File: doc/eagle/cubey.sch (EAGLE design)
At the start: 25 parts, among them K1 PIN20X2

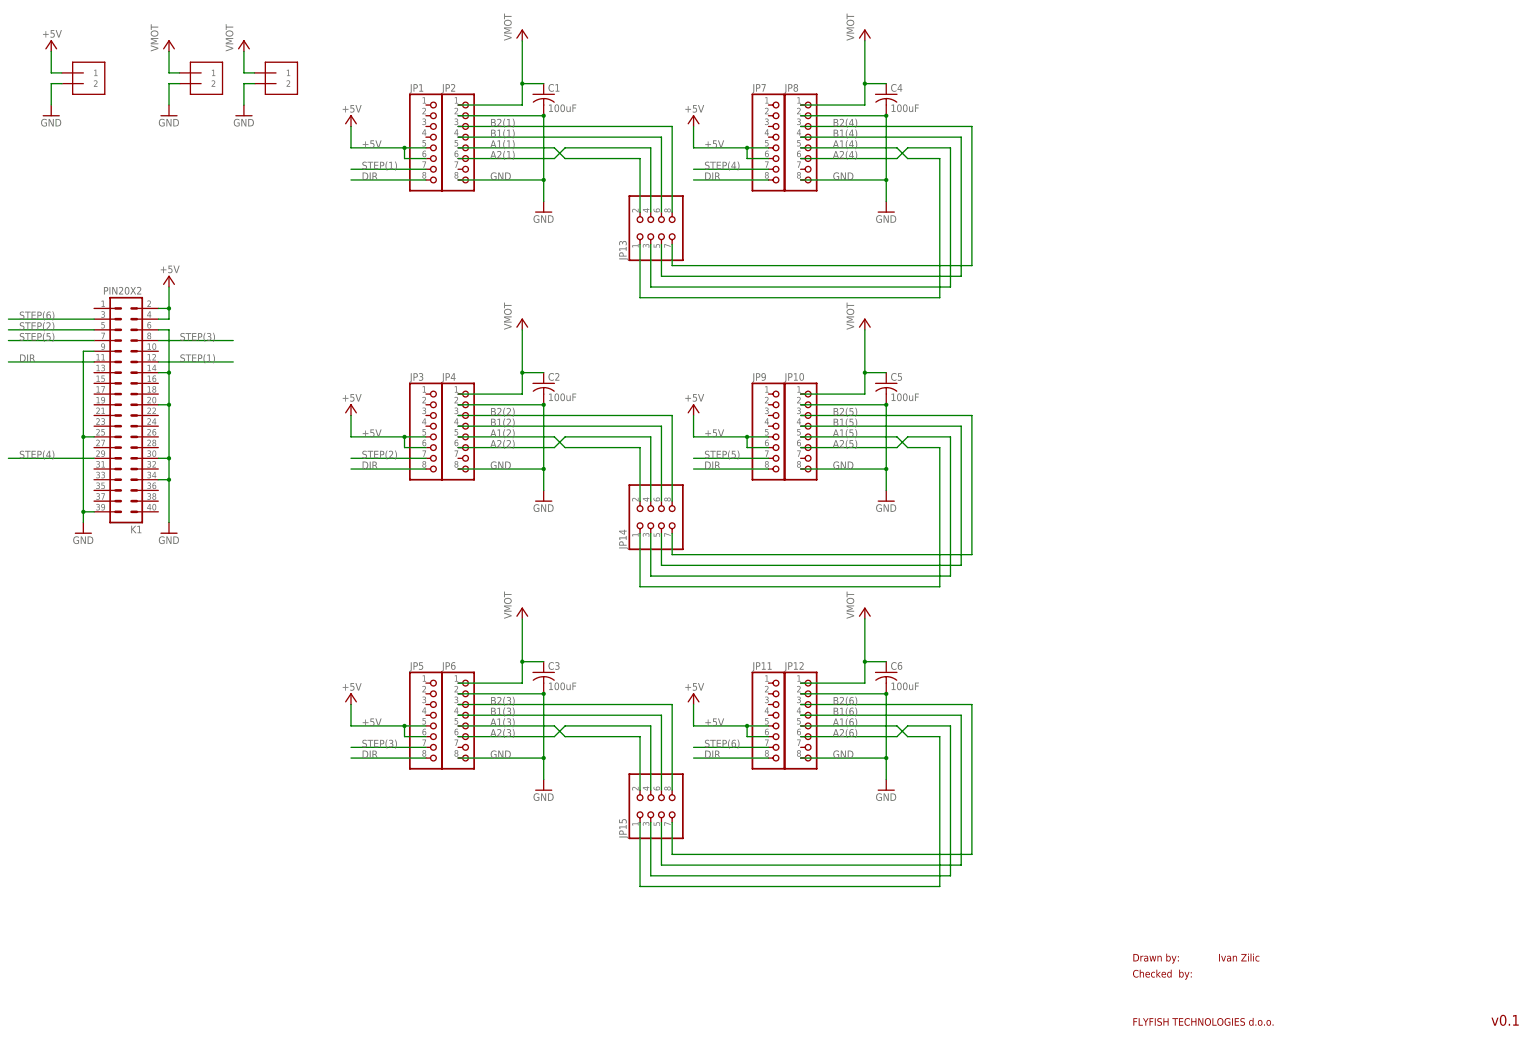
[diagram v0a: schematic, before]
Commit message: Added Solder jumpers for M0, M1 and M2
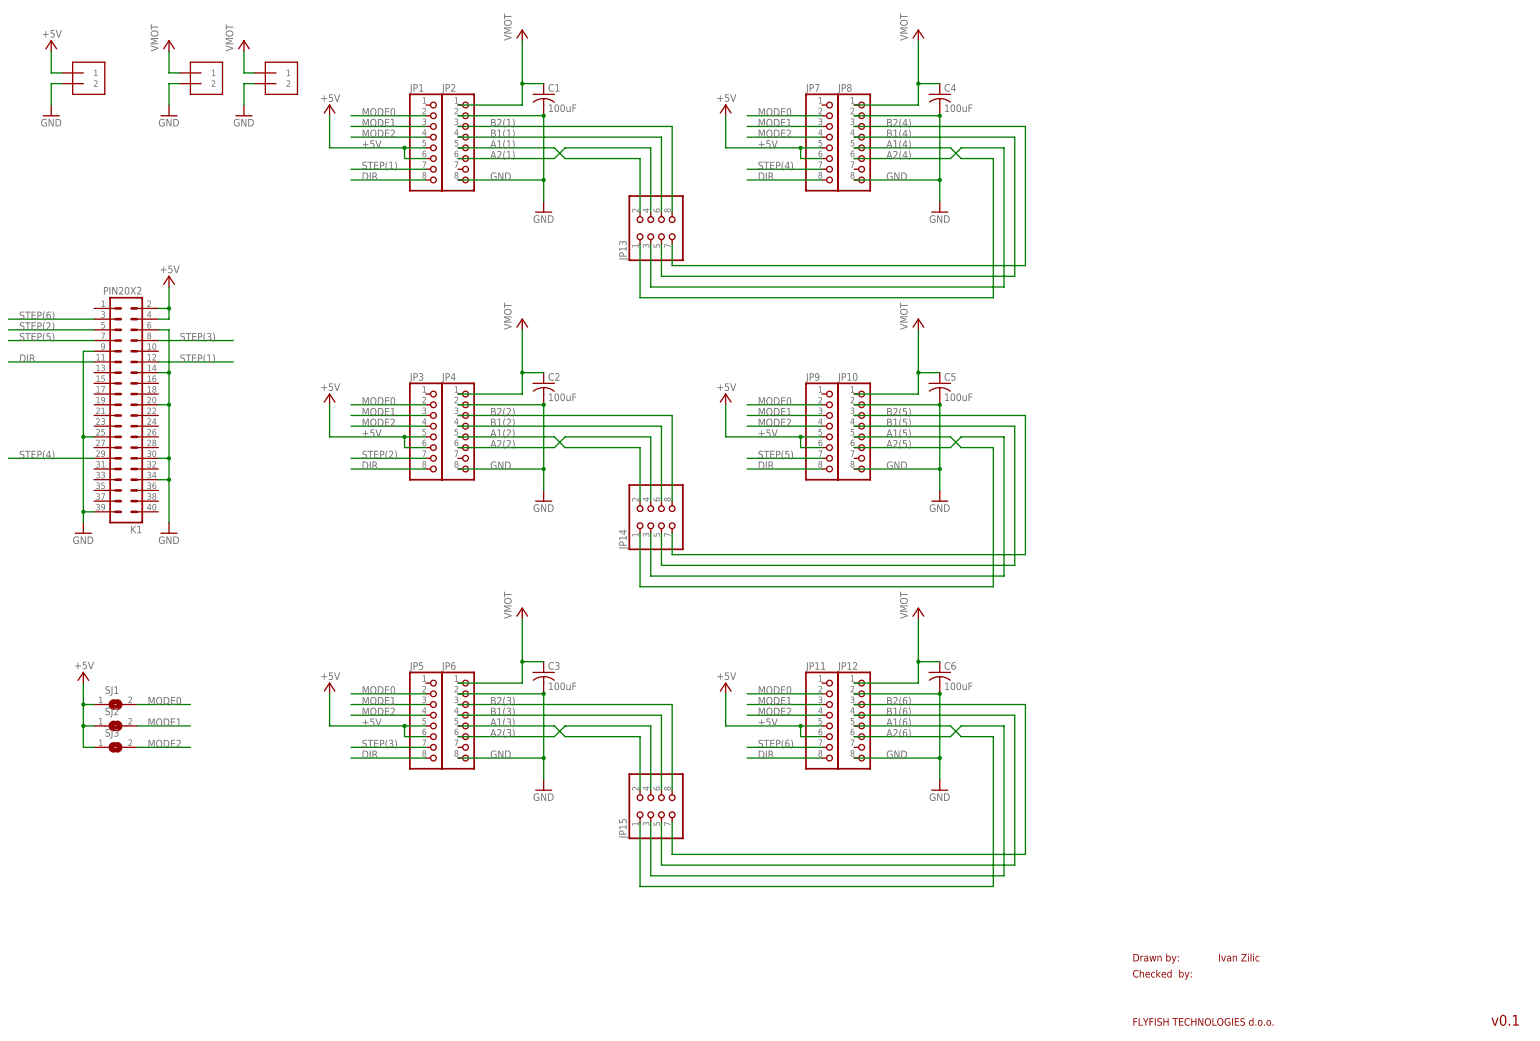
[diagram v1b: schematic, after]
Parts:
- added SJ1, SJ2, SJ3: (no value), jumper:SJ
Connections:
- new net MODE0: JP1.2, JP11.2, JP3.2, JP5.2, JP7.2, JP9.2, SJ1.2
- new net MODE1: JP1.3, JP11.3, JP3.3, JP5.3, JP7.3, JP9.3, SJ2.2
- new net MODE2: JP1.4, JP11.4, JP3.4, JP5.4, JP7.4, JP9.4, SJ3.2
- net +5V: now also SJ1.1, SJ2.1, SJ3.1
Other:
- moved on the sheet: C4, C5, C6, JP10, JP11, JP12, JP7, JP8, JP9

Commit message: Rename signals in Cubey PCB design. Finalized V2 with ENABLE pin.
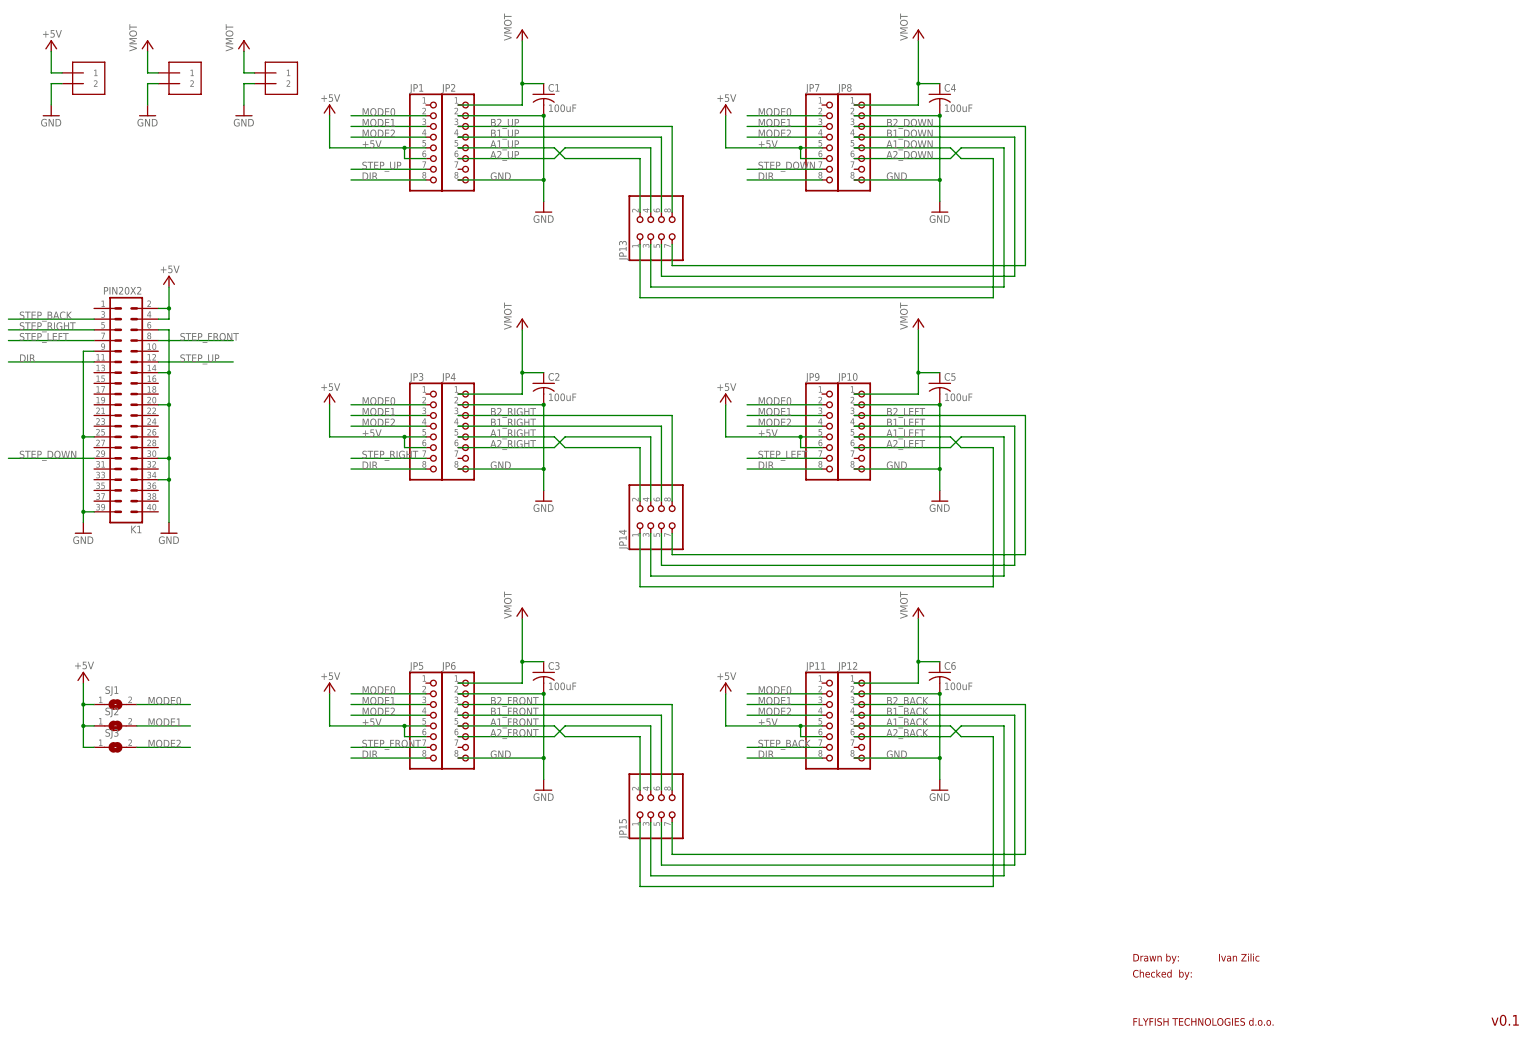
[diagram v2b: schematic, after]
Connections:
- net A1(1) renamed A1_UP
- net A1(2) renamed A1_RIGHT
- net A1(3) renamed A1_FRONT
- net A1(4) renamed A1_DOWN
- net A1(5) renamed A1_LEFT
- net A1(6) renamed A1_BACK
- net A2(1) renamed A2_UP
- net A2(2) renamed A2_RIGHT
- net A2(3) renamed A2_FRONT
- net A2(4) renamed A2_DOWN
- net A2(5) renamed A2_LEFT
- net A2(6) renamed A2_BACK
- net B1(1) renamed B1_UP
- net B1(2) renamed B1_RIGHT
- net B1(3) renamed B1_FRONT
- net B1(4) renamed B1_DOWN
- net B1(5) renamed B1_LEFT
- net B1(6) renamed B1_BACK
- net B2(1) renamed B2_UP
- net B2(2) renamed B2_RIGHT
- net B2(3) renamed B2_FRONT
- net B2(4) renamed B2_DOWN
- net B2(5) renamed B2_LEFT
- net B2(6) renamed B2_BACK
- net STEP(1) renamed STEP_UP
- net STEP(2) renamed STEP_RIGHT
- net STEP(3) renamed STEP_FRONT
- net STEP(4) renamed STEP_DOWN
- net STEP(5) renamed STEP_LEFT
- net STEP(6) renamed STEP_BACK
